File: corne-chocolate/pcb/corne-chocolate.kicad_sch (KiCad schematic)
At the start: 87 parts, among them J1 MJ-4PP-9, J2 OLED, J3 LED, P1 i2c-pin, P2 i2c-pin, SW1 SW_PUSH, SW10 SW_PUSH, SW11 SW_PUSH, SW12 SW_PUSH, SW13 SW_PUSH, SW14 SW_PUSH, SW15 SW_PUSH, SW16 SW_PUSH, SW17 SW_PUSH, SW18 SW_PUSH, SW19 SW_PUSH, SW2 SW_PUSH, SW20 SW_PUSH, SW21 SW_PUSH, SW3 SW_PUSH, SW4 SW_PUSH, SW5 SW_PUSH, SW6 SW_PUSH, SW7 SW_PUSH, SW8 SW_PUSH, SW9 SW_PUSH, U1 ProMicro

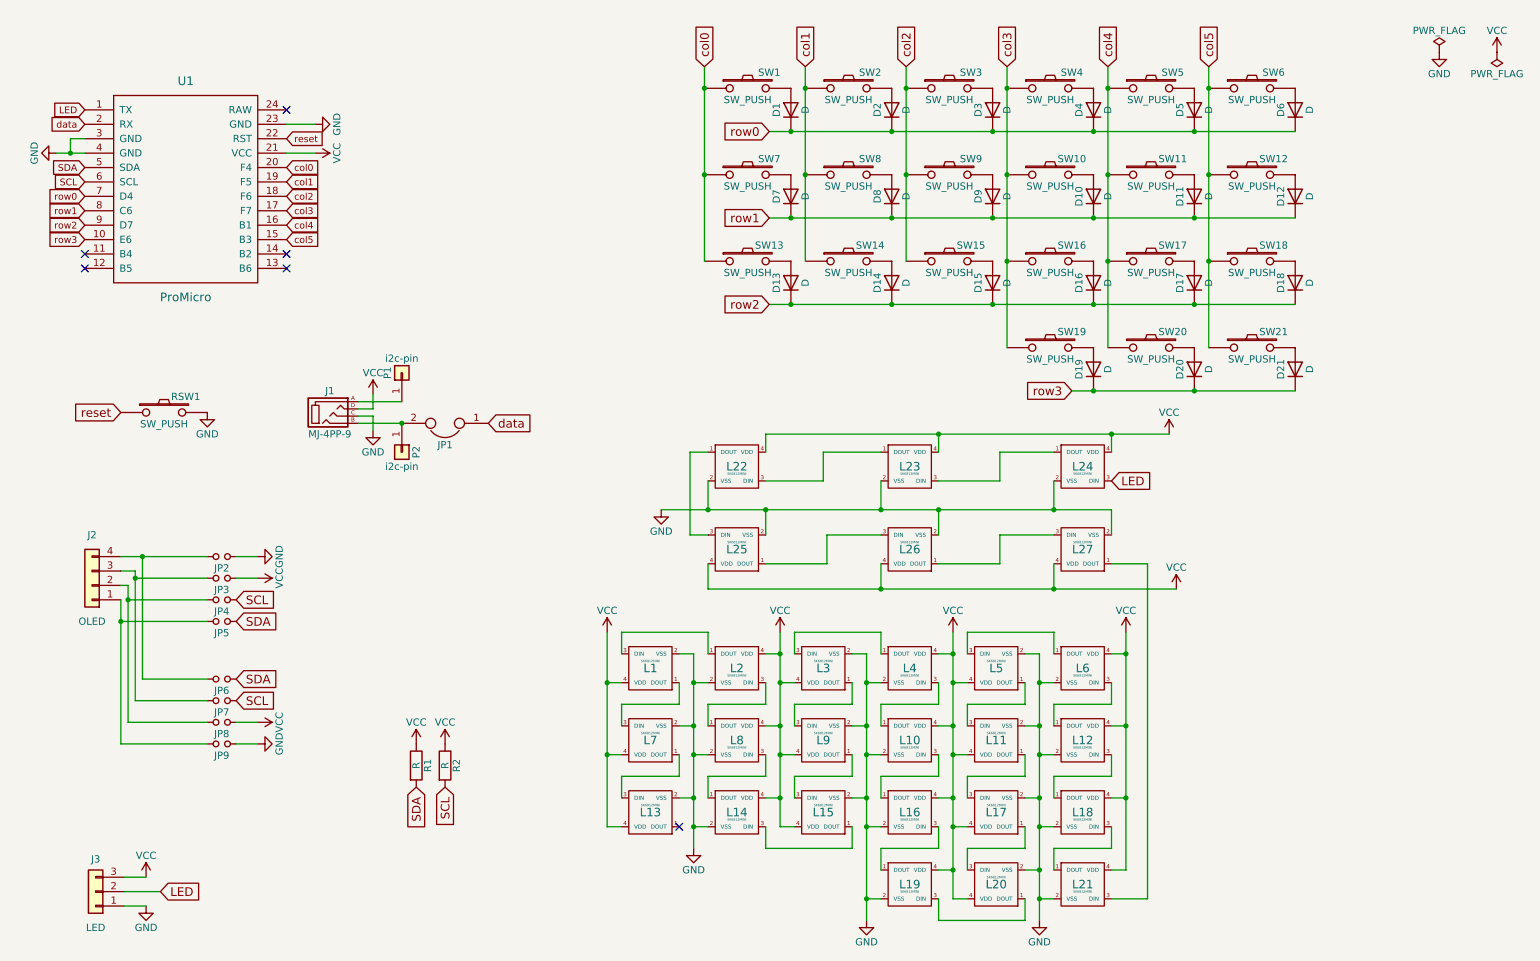
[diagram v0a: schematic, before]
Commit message: add nice!view battery connector, reset and power switch to schematics
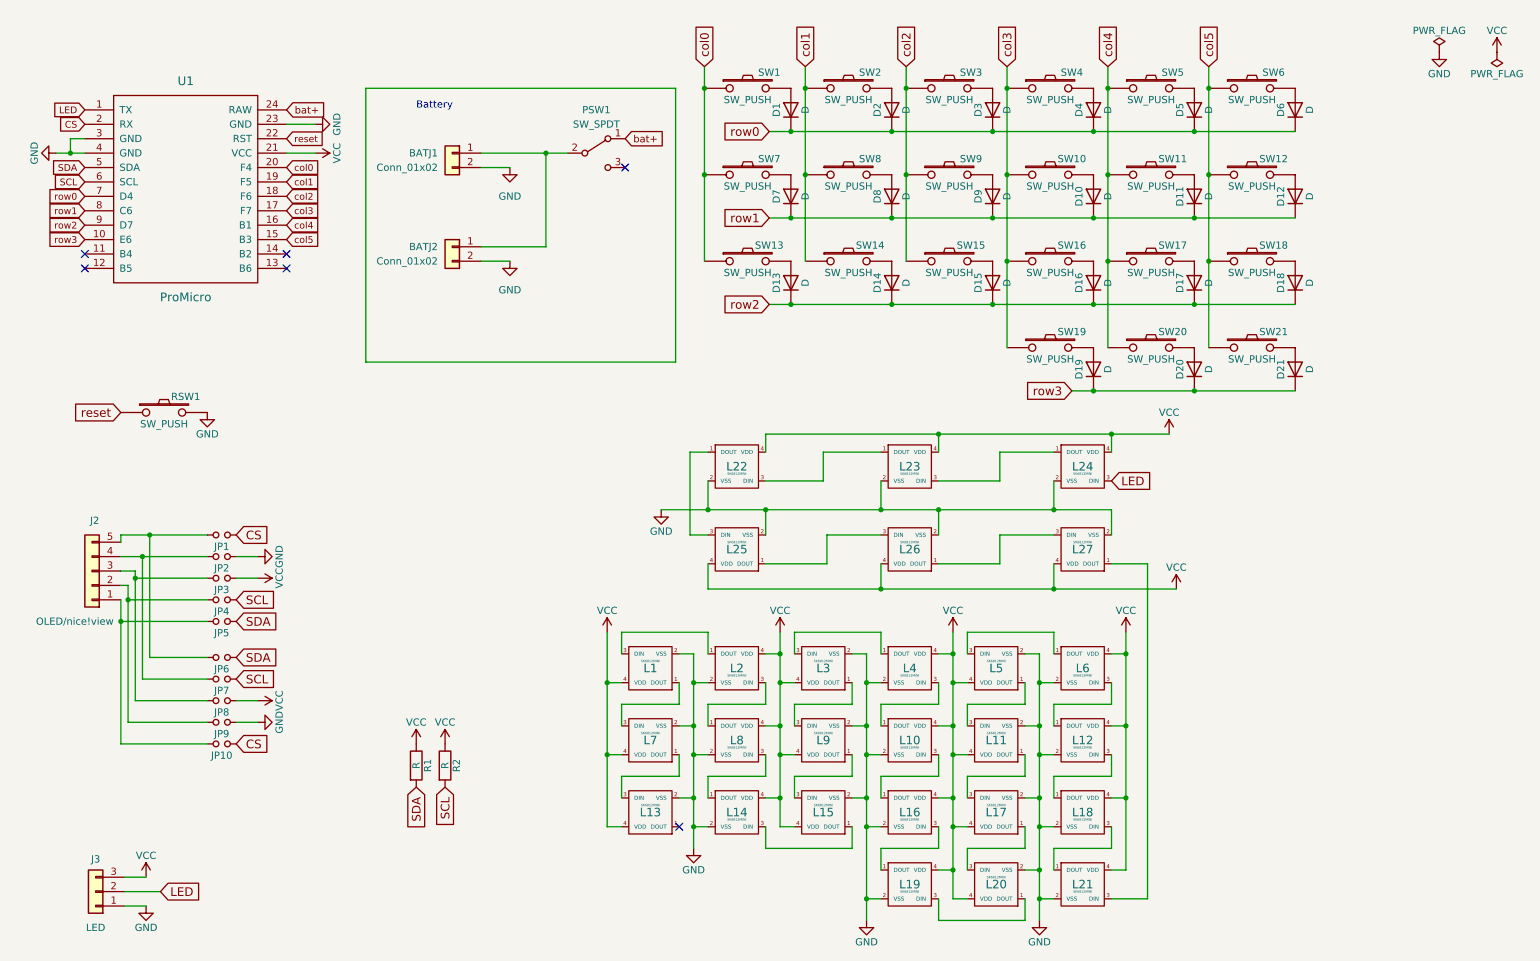
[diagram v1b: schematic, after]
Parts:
- removed J1: MJ-4PP-9, kbd:MJ-4PP-9, symbol corne-chocolate-rescue:MJ-4PP-9-kbd
- removed J2: OLED, kbd:OLED, symbol Connector_Generic:Conn_01x04
- removed JP1: (no value), kbd:JPC2, symbol corne-chocolate-rescue:Jumper-Device
- removed P1, P2: i2c-pin, kbd:1pin_conn, symbol Connector_Generic:Conn_01x01
- added BATJ1: Conn_01x02, Connector_JST:JST_PH_S2B-PH-K_1x02_P2.00mm_Horizontal, symbol Connector_Generic:Conn_01x02
- added BATJ2: Conn_01x02, Connector_PinSocket_2.54mm:PinSocket_1x02_P2.54mm_Vertical, symbol Connector_Generic:Conn_01x02
- added J2: OLED/nice!view, Connector_PinSocket_2.54mm:PinSocket_1x05_P2.54mm_Vertical, symbol Connector_Generic:Conn_01x05
- added JP1, JP6: (no value), kbd:Jumper, symbol corne-chocolate-rescue:Jumper_NO_Small-Device
- added PSW1: SW_SPDT, kbd:SPDT_C128955, symbol Switch:SW_SPDT
- RSW1: footprint kbd:ResetSW -> kbd:RSW_SKSNLAE010
- renumbered JP9 to JP10, JP6 to JP7, JP7 to JP8, JP8 to JP9
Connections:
- net GND: now also JP9.1, BATJ1.2 (Pin_2), BATJ2.2 (Pin_2); no longer JP10.1
- net SCL: now also JP7.1; no longer JP8.1
- net SDA: now also JP6.1; no longer JP7.1
- net VCC: now also JP8.1; no longer JP9.1
- net bat+: now reaches U1.24 (RAW)
- net bat+: now also PSW1.1 (A)
- net at JP10.2, JP5.2: now also J2.1 (Pin_1)
- net at JP4.2, JP9.2: now also J2.2 (Pin_2)
- net at JP3.2, JP8.2: now also J2.3 (Pin_3)
- net at JP2.2, JP7.2: now also J2.4 (Pin_4)
- net data renamed CS
- net CS: now also JP10.1, JP1.1
- new net: BATJ1.1 (Pin_1), BATJ2.1 (Pin_1), PSW1.2 (B)
- new net: J2.5 (Pin_5), JP1.2, JP6.2
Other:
- note added: "Battery"
